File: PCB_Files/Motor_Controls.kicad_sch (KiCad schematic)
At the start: 26 parts, among them M1 Left_Front_Motor, M2 Left_Rear_Motor, M3 Right_Front_Motor, M4 Right_Rear_Motor, U2 TB6612FNG, U3 TB6612FNG

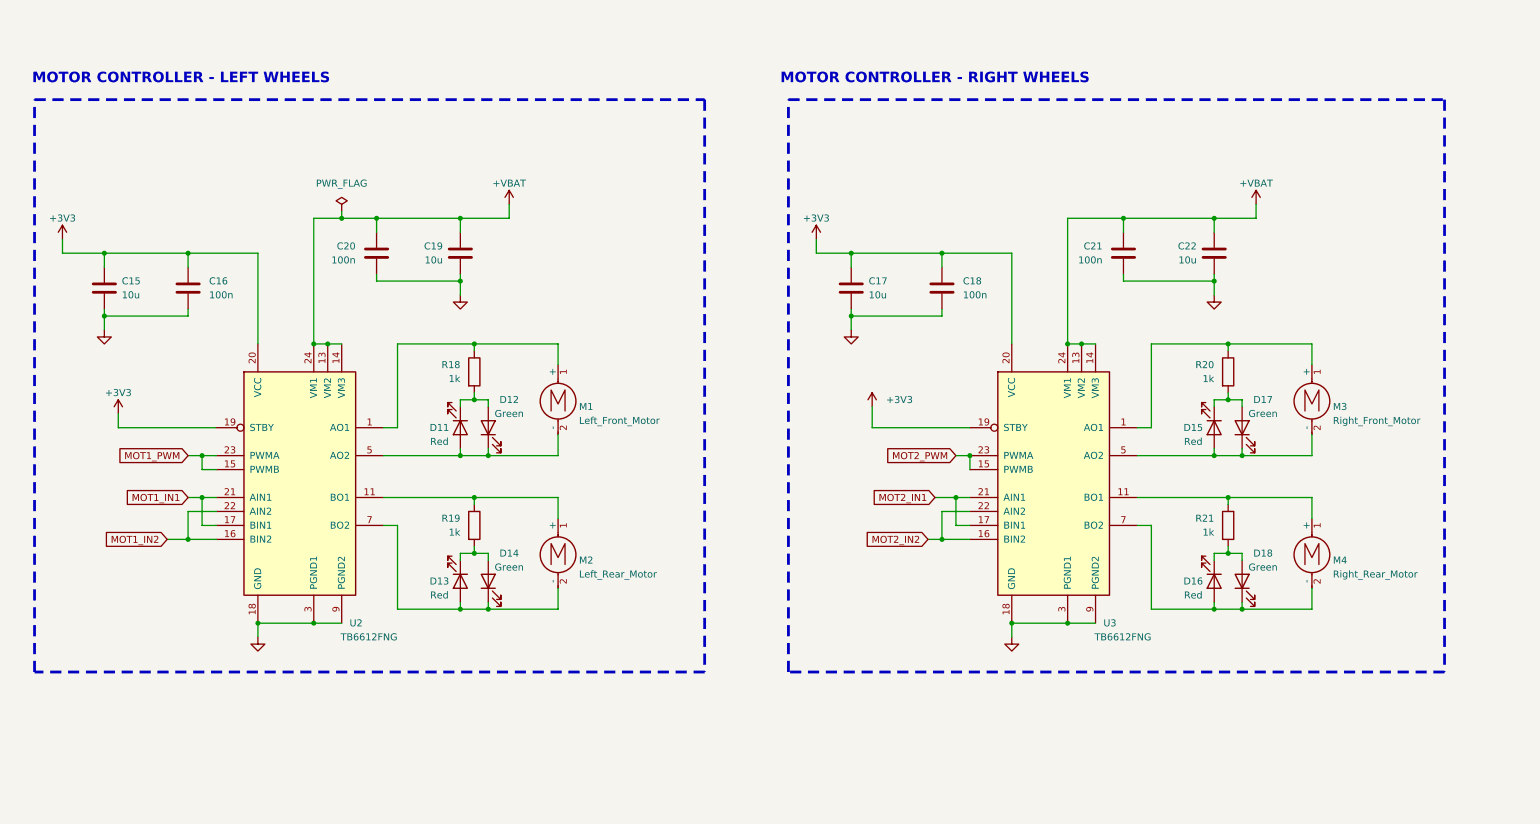
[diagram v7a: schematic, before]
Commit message: Cleaned up motor controller schematic by seperating power decoupling for both motor controllers, seperated SGND and PGND, and rearranged input pin wiring for clearity.
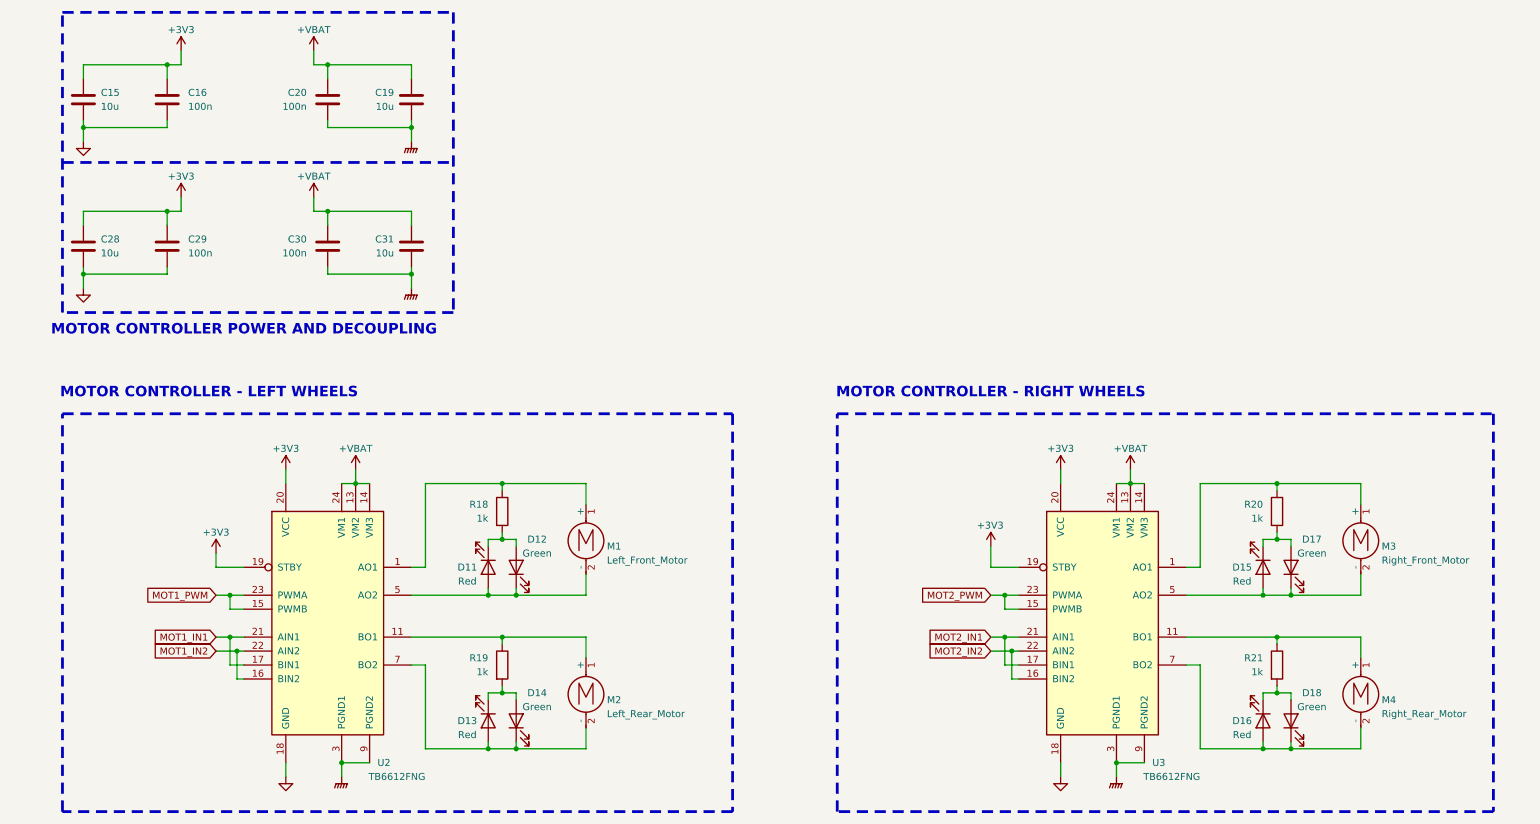
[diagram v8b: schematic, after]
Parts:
- removed C17, C22: 10u, Capacitor_SMD:C_0603_1608Metric, symbol Device:C
- removed C18, C21: 100n, Capacitor_SMD:C_0603_1608Metric, symbol Device:C
- added C28, C31: 10u, Capacitor_SMD:C_0603_1608Metric, symbol Device:C
- added C29, C30: 100n, Capacitor_SMD:C_0603_1608Metric, symbol Device:C
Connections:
- net +3V3: now also C28.1, C29.1
- net +VBAT: now also C30.1, C31.1
- net GND: now also C28.2, C29.2; no longer C19.2, C20.2, U2.10 (PGND2), U2.3 (PGND1), U2.4 (PGND1), U2.9 (PGND2), U3.10 (PGND2), U3.3 (PGND1), U3.4 (PGND1), U3.9 (PGND2)
- new net GNDPWR: C19.2, C20.2, C30.2, C31.2, U2.10 (PGND2), U2.3 (PGND1), U2.4 (PGND1), U2.9 (PGND2), U3.10 (PGND2), U3.3 (PGND1), U3.4 (PGND1), U3.9 (PGND2)
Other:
- note added: "MOTOR CONTROLLER POWER AND DECOUPLING"
- moved on the sheet: C15, C16, C19, C20, D11, D12, D13, D14, D15, D16, D17, D18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
